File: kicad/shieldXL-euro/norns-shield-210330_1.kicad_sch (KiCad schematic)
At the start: 43 parts, among them J1 NRJ6HF, J2 NRJ6HF, J4 NRJ6HF, J5 NRJ6HF, Q1 ASFL1-12.288MHZ-LCS-T, U1 CS4270, U11 TPS793475DBVR, X1 RASPI_BOARD_B+#_E3

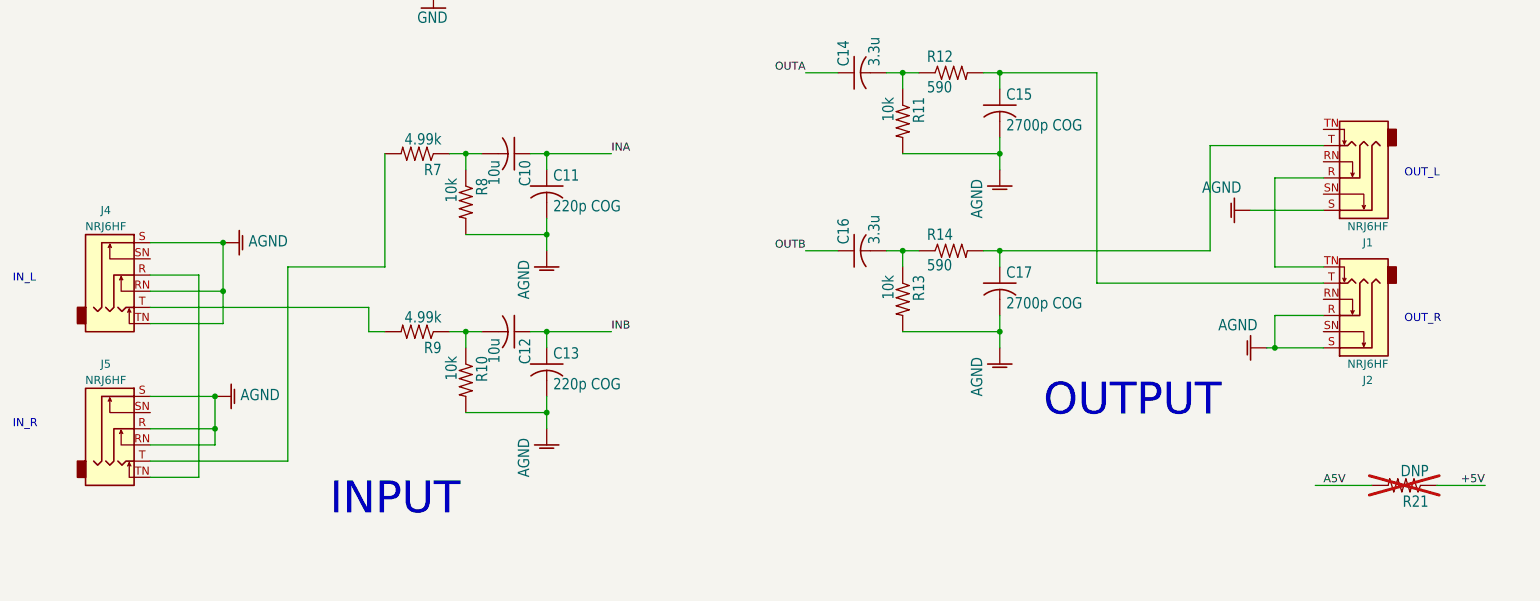
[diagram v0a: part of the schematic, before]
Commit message: Remove the desktop I/O: 6.35 mm jacks, PJ-320B MIDI jacks, A/B slide switch
tools/strip_shield_io.py takes J1, J2, J4, J5 off sheet 1 and J3, J6, S1 off
sheet 2, puts a global label wherever a signal reached them (IN_L_LINE,
IN_R_LINE, OUT_L_LINE, OUT_R_LINE, MIDI_OUT_SRC, MIDI_OUT_SNK, MIDI_IN_TIP,
MIDI_IN_RING), and prunes the wires left hanging. Checked against the
baseline netlist: every net keeps exactly its connections, less the removed
parts' pins. The Eurorack I/O that replaces them comes next.

Co-Authored-By: Claude Opus 5.5 <noreply@anthropic.com>
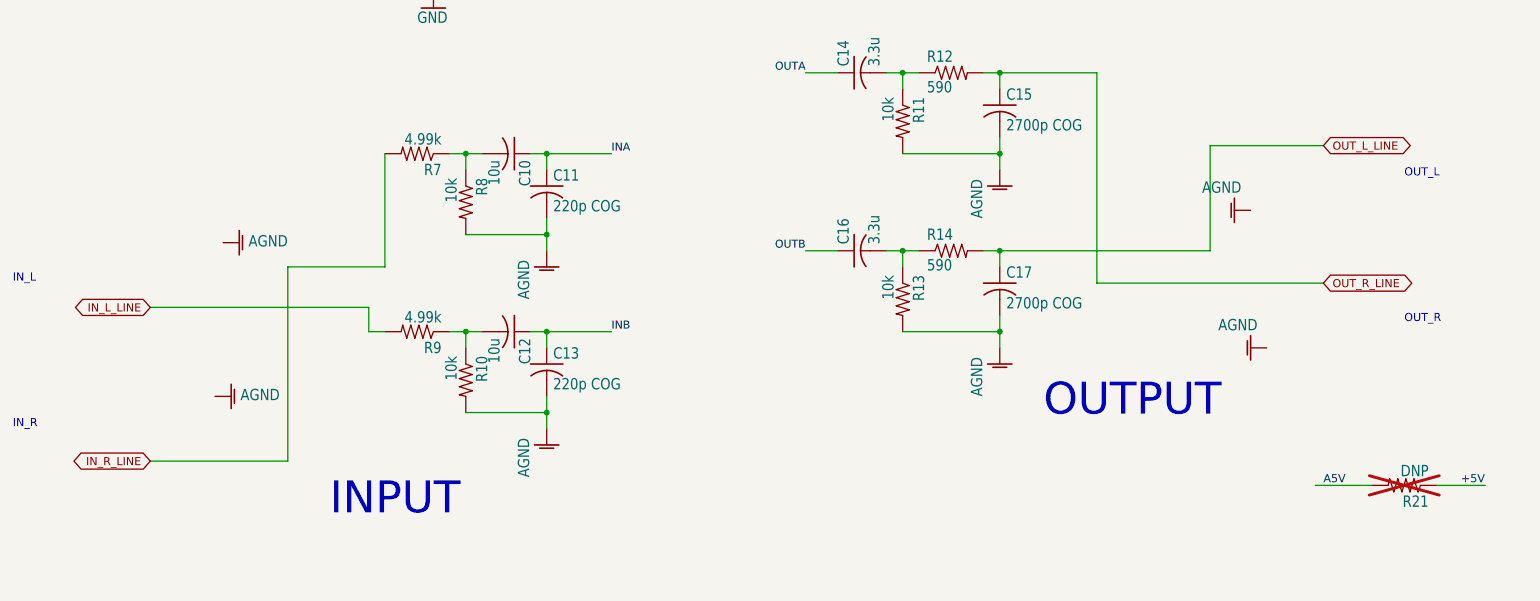
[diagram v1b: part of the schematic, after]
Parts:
- removed J1, J2, J4, J5: NRJ6HF, ShieldXL:Jack_6.35mm_Neutrik_NRJ6HF_Horizontal, symbol Connector_Audio:NRJ6HF
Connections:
- net OUT_L_LINE: now reaches C17.1, R14.2
- net IN_R_LINE: now reaches R7.2
- net OUT_R_LINE: now reaches C15.1, R12.2
- net IN_L_LINE: now reaches R9.2
